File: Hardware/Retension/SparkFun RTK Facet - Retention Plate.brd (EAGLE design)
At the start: 100 x 58 mm, 6 parts

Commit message: Add retention plate gerbers v10
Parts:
- added U$4: (no value), output:RTK5#SVG0
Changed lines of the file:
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@@
 <setting verticaltext="up"/>
 </settings>
-<grid distance="1" unitdist="mm" unit="mm" style="lines" multiple="1" display="yes" altdistance="0.1" altunitdist="mm" altunit="mm"/>
+<grid distance="0.05" unitdist="inch" unit="inch" style="lines" multiple="1" display="yes" altdistance="0.005" altunitdist="inch" altunit="inch"/>
 <layers>
 <layer number="1" name="Top" color="4" fill="1" visible="yes" active="yes"/>
@@
 <layer number="23" name="tOrigins" color="15" fill="1" visible="yes" active="yes"/>
 <layer number="24" name="bOrigins" color="15" fill="1" visible="yes" active="yes"/>
-<layer number="25" name="tNames" color="7" fill="1" visible="no" active="yes"/>
-<layer number="26" name="bNames" color="7" fill="1" visible="no" active="yes"/>
-<layer number="27" name="tValues" color="7" fill="1" visible="no" active="yes"/>
-<layer number="28" name="bValues" color="7" fill="1" visible="no" active="yes"/>
-<layer number="29" name="tStop" color="7" fill="3" visible="no" active="yes"/>
-<layer number="30" name="bStop" color="7" fill="6" visible="no" active="yes"/>
-<layer number="31" name="tCream" color="7" fill="4" visible="no" active="yes"/>
-<layer number="32" name="bCream" color="7" fill="5" visible="no" active="yes"/>
-<layer number="33" name="tFinish" color="6" fill="3" visible="no" active="yes"/>
-<layer number="34" name="bFinish" color="6" fill="6" visible="no" active="yes"/>
-<layer number="35" name="tGlue" color="7" fill="4" visible="no" active="yes"/>
-<layer number="36" name="bGlue" color="7" fill="5" visible="no" active="yes"/>
-<layer number="37" name="tTest" color="7" fill="1" visible="no" active="yes"/>
-<layer number="38" name="bTest" color="7" fill="1" visible="no" active="yes"/>
-<layer number="39" name="tKeepout" color="4" fill="11" visible="no" active="yes"/>
-<layer number="40" name="bKeepout" color="1" fill="11" visible="no" active="yes"/>
-<layer number="41" name="tRestrict" color="4" fill="10" visible="no" active="yes"/>
-<layer number="42" name="bRestrict" color="1" fill="10" visible="no" active="yes"/>
-<layer number="43" name="vRestrict" color="2" fill="10" visible="no" active="yes"/>
-<layer number="44" name="Drills" color="7" fill="1" visible="no" active="yes"/>
+<layer number="25" name="tNames" color="7" fill="1" visible="yes" active="yes"/>
+<layer number="26" name="bNames" color="7" fill="1" visible="yes" active="yes"/>
+<layer number="27" name="tValues" color="7" fill="1" visible="yes" active="yes"/>
+<layer number="28" name="bValues" color="7" fill="1" visible="yes" active="yes"/>
+<layer number="29" name="tStop" color="7" fill="3" visible="yes" active="yes"/>
+<layer number="30" name="bStop" color="7" fill="6" visible="yes" active="yes"/>
+<layer number="31" name="tCream" color="7" fill="4" visible="yes" active="yes"/>
+<layer number="32" name="bCream" color="7" fill="5" visible="yes" active="yes"/>
+<layer number="33" name="tFinish" color="6" fill="3" visible="yes" active="yes"/>
+<layer number="34" name="bFinish" color="6" fill="6" visible="yes" active="yes"/>
+<layer number="35" name="tGlue" color="7" fill="4" visible="yes" active="yes"/>
+<layer number="36" name="bGlue" color="7" fill="5" visible="yes" active="yes"/>
+<layer number="37" name="tTest" color="7" fill="1" visible="yes" active="yes"/>
+<layer number="38" name="bTest" color="7" fill="1" visible="yes" active="yes"/>
+<layer number="39" name="tKeepout" color="4" fill="11" visible="yes" active="yes"/>
+<layer number="40" name="bKeepout" color="1" fill="11" visible="yes" active="yes"/>
+<layer number="41" name="tRestrict" color="4" fill="10" visible="yes" active="yes"/>
+<layer number="42" name="bRestrict" color="1" fill="10" visible="yes" active="yes"/>
+<layer number="43" name="vRestrict" color="2" fill="10" visible="yes" active="yes"/>
+<layer number="44" name="Drills" color="7" fill="1" visible="yes" active="yes"/>
 <layer number="45" name="Holes" color="7" fill="1" visible="yes" active="yes"/>
-<layer number="46" name="Milling" color="3" fill="1" visible="no" active="yes"/>
+<layer number="46" name="Milling" color="3" fill="1" visible="yes" active="yes"/>
 <layer number="47" name="Measures" color="7" fill="1" visible="yes" active="yes"/>
-<layer number="48" name="Document" color="7" fill="1" visible="no" active="yes"/>
-<layer number="49" name="Reference" color="7" fill="1" visible="no" active="yes"/>
-<layer number="50" name="dxf" color="7" fill="1" visible="no" active="yes"/>
+<layer number="48" name="Document" color="7" fill="1" visible="yes" active="yes"/>
+<layer number="49" name="Reference" color="7" fill="1" visible="yes" active="yes"/>
+<layer number="50" name="dxf" color="7" fill="1" visible="yes" active="yes"/>
 <layer number="51" name="tDocu" color="6" fill="1" visible="yes" active="yes"/>
-<layer number="52" name="bDocu" color="7" fill="1" visible="no" active="yes"/>
+<layer number="52" name="bDocu" color="7" fill="1" visible="yes" active="yes"/>
 <layer number="91" name="Nets" color="2" fill="1" visible="no" active="no"/>
 <layer number="92" name="Busses" color="1" fill="1" visible="no" active="no"/>
@@
 <element name="U$2" library="output" package="RTK_FACET0" value="" x="50" y="8" smashed="yes"/>
 <element name="U$3" library="SparkFun-Aesthetics" package="ORDERING_INSTRUCTIONS" value="" x="142.24" y="50.8" smashed="yes"/>
+<element name="U$4" library="output" package="RTK5#SVG0" value="" x="49.53" y="29.21" smashed="yes"/>
 </elements>
 <signals>

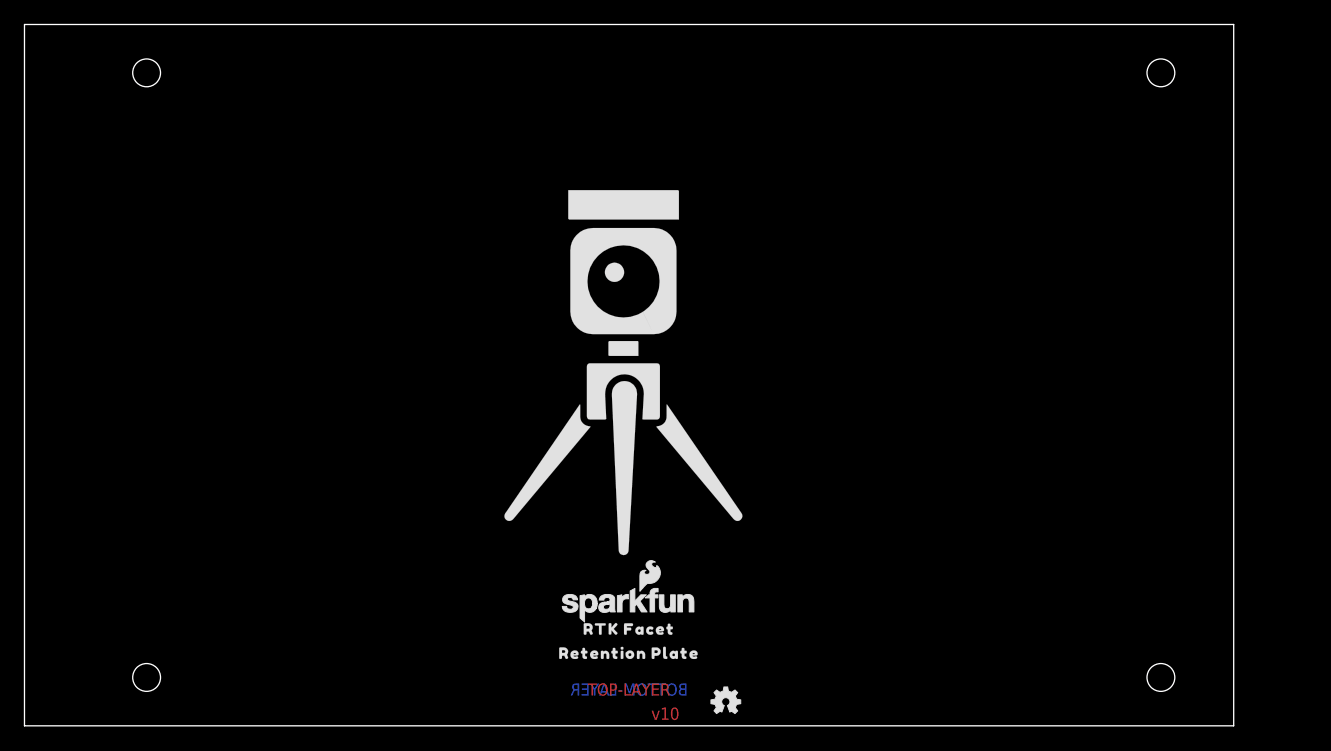
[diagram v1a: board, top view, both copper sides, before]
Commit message: Extend retention plate length to make it reversible. Add LTE only sticker.
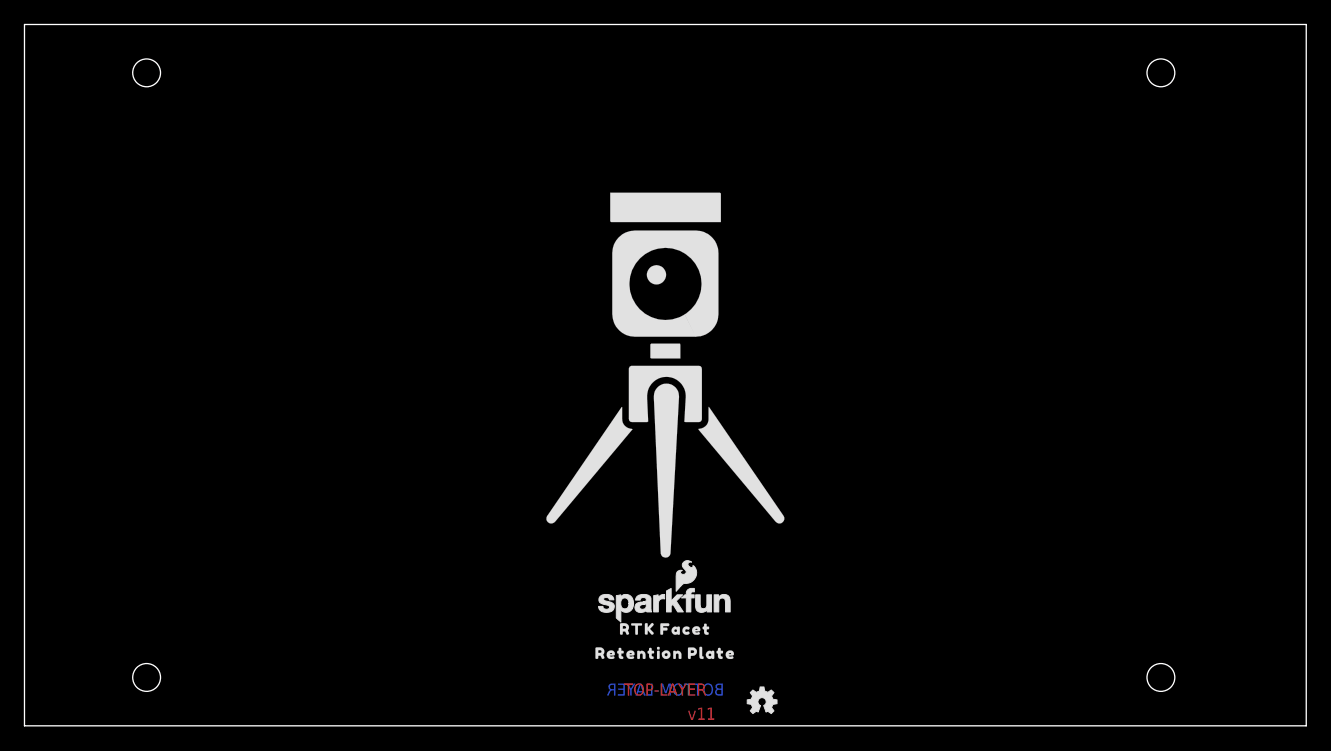
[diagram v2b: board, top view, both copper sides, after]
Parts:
- moved U$4 3.48 mm to (53.0, 29.0)
- moved LOGO3 3.00 mm to (61.0, 2.00)
- moved LOGO5 3.00 mm to (53.0, 10.0)
- moved U$1 3.00 mm to (53.0, 6.00)
- moved U$2 3.00 mm to (53.0, 8.00)
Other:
- board size 100 x 58 mm -> 106 x 58 mm
- board text added: "v11"
- board text removed: "v10"
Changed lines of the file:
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@@
 <setting verticaltext="up"/>
 </settings>
-<grid distance="0.05" unitdist="inch" unit="inch" style="lines" multiple="1" display="yes" altdistance="0.005" altunitdist="inch" altunit="inch"/>
+<grid distance="1" unitdist="mm" unit="mm" style="lines" multiple="1" display="yes" altdistance="0.1" altunitdist="mm" altunit="mm"/>
 <layers>
 <layer number="1" name="Top" color="4" fill="1" visible="yes" active="yes"/>
@@
 <board>
 <plain>
-<text x="53" y="1" size="1.016" layer="1" font="vector" ratio="20" rot="R180" align="center">v10</text>
-<wire x1="50" y1="60" x2="50" y2="-2" width="0.05" layer="51"/>
+<text x="56" y="1" size="1.016" layer="1" font="vector" ratio="20" rot="R180" align="center">v11</text>
+<wire x1="53" y1="60" x2="53" y2="-2" width="0.05" layer="51"/>
 <wire x1="0" y1="0" x2="0" y2="58" width="0.05" layer="20"/>
-<wire x1="0" y1="58" x2="100" y2="58" width="0.05" layer="20"/>
-<wire x1="100" y1="58" x2="100" y2="0" width="0.05" layer="20"/>
-<wire x1="100" y1="0" x2="0" y2="0" width="0.05" layer="20"/>
+<wire x1="0" y1="58" x2="106" y2="58" width="0.05" layer="20"/>
+<wire x1="106" y1="58" x2="106" y2="0" width="0.05" layer="20"/>
+<wire x1="106" y1="0" x2="0" y2="0" width="0.05" layer="20"/>
 <hole x="93.98" y="4" drill="2.3"/>
 <hole x="10.1" y="4" drill="2.3"/>
@@
 <hole x="10.1" y="54" drill="2.3"/>
 <hole x="93.98" y="54" drill="2.3"/>
-<text x="50" y="3" size="1" layer="1" font="vector" ratio="20" align="center">TOP-LAYER</text>
-<text x="50" y="3" size="1" layer="16" font="vector" ratio="20" rot="MR0" align="center">BOTTOM-LAYER</text>
-<wire x1="-2" y1="29" x2="102" y2="29" width="0.05" layer="51"/>
+<text x="53" y="3" size="1" layer="1" font="vector" ratio="20" align="center">TOP-LAYER</text>
+<text x="53" y="3" size="1" layer="16" font="vector" ratio="20" rot="MR0" align="center">BOTTOM-LAYER</text>
+<wire x1="-2" y1="29" x2="108" y2="29" width="0.05" layer="51"/>
 <dimension x1="10.1" y1="4" x2="0" y2="0" x3="5.05" y3="-2" textsize="0.5" textratio="15" layer="47" dtype="horizontal" width="0.05"/>
-<dimension x1="100" y1="0" x2="93.98" y2="4" x3="96.99" y3="-2" textsize="0.5" textratio="15" layer="47" dtype="horizontal" width="0.05"/>
-<dimension x1="100" y1="0" x2="93.98" y2="4" x3="103" y3="2" textsize="0.5" textratio="15" layer="47" dtype="vertical" width="0.05"/>
+<dimension x1="106" y1="0" x2="93.98" y2="4" x3="99.99" y3="-2" textsize="0.5" textratio="15" layer="47" dtype="horizontal" width="0.05"/>
+<dimension x1="100" y1="0" x2="93.98" y2="4" x3="108.5" y3="2" textsize="0.5" textratio="15" layer="47" dtype="vertical" width="0.05"/>
 <dimension x1="0" y1="0" x2="10.1" y2="4" x3="-3" y3="2" textsize="0.5" textratio="15" layer="47" dtype="vertical" width="0.05"/>
 <dimension x1="0" y1="58" x2="10.1" y2="54" x3="-2" y3="56" textsize="0.5" textratio="15" layer="47" dtype="vertical" width="0.05"/>
 <dimension x1="0" y1="0" x2="0" y2="58" x3="-6" y3="29" textsize="1" layer="47" width="0.1"/>
-<dimension x1="0" y1="58" x2="100" y2="58" x3="50" y3="63" textsize="1" layer="47" width="0.1"/>
+<dimension x1="0" y1="58" x2="106" y2="58" x3="53" y3="63" textsize="1" layer="47" width="0.1"/>
 </plain>
 <attributes>
@@
 <attribute name="REV" value="" x="-2.57" y="-29.5" size="1.778" layer="27" display="off"/>
 </element>
-<element name="LOGO3" library="SparkFun-Aesthetics" package="OSHW-LOGO-MINI" value="OSHW-LOGOMINI" x="58" y="2" smashed="yes"/>
-<element name="LOGO5" library="SparkFun-Aesthetics" package="SFE_LOGO_NAME_FLAME_.1" value="SFE_LOGO_NAME_FLAME.1_INCH" x="50" y="10" smashed="yes"/>
-<element name="U$1" library="output" package="RETENTION_PLATE1" value="" x="50" y="6" smashed="yes"/>
-<element name="U$2" library="output" package="RTK_FACET0" value="" x="50" y="8" smashed="yes"/>
+<element name="LOGO3" library="SparkFun-Aesthetics" package="OSHW-LOGO-MINI" value="OSHW-LOGOMINI" x="61" y="2" smashed="yes"/>
+<element name="LOGO5" library="SparkFun-Aesthetics" package="SFE_LOGO_NAME_FLAME_.1" value="SFE_LOGO_NAME_FLAME.1_INCH" x="53" y="10" smashed="yes"/>
+<element name="U$1" library="output" package="RETENTION_PLATE1" value="" x="53" y="6" smashed="yes"/>
+<element name="U$2" library="output" package="RTK_FACET0" value="" x="53" y="8" smashed="yes"/>
 <element name="U$3" library="SparkFun-Aesthetics" package="ORDERING_INSTRUCTIONS" value="" x="142.24" y="50.8" smashed="yes"/>
-<element name="U$4" library="output" package="RTK5#SVG0" value="" x="49.53" y="29.21" smashed="yes"/>
+<element name="U$4" library="output" package="RTK5#SVG0" value="" x="53" y="29" smashed="yes"/>
 </elements>
 <signals>
